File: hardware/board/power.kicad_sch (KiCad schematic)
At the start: 1 part, among them U4 RK809-5

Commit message: added stuff
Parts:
- added C10, C11, C12, C13, C14, C15, C20, C8, C9: 100nF X5R 10V, Capacitor_SMD:C_0402_1005Metric, symbol Device:C
- added C16, C17: 220pF C0G 25V, Capacitor_SMD:C_0402_1005Metric, symbol Device:C
- added C18: 1uF X5R 10V, Capacitor_SMD:C_0402_1005Metric, symbol Device:C
- added C19, C7: 10uF X5R 10V, Capacitor_SMD:C_0603_1608Metric, symbol Device:C
- added C21, C23, C3, C4, C5, C6: 10uF X5R 25V, Capacitor_SMD:C_0805_2012Metric, symbol Device:C
- added C22: 100pF C0G 50V, Capacitor_SMD:C_0402_1005Metric, symbol Device:C
- added C24: 4.7uF X5R 10V, Capacitor_SMD:C_0402_1005Metric, symbol Device:C
- added C25: 47nF X5R 25V, Capacitor_SMD:C_0402_1005Metric, symbol Device:C
- added C26, C27, C28: 10uF X5R 10V, Capacitor_SMD:C_0805_2012Metric, symbol Device:C
- added D1, D2, D3, D4, D5: BZT52C5V1_C173407, lcsc:SOD-123_L2.7-W1.6-LS3.7-RD, symbol lcsc:BZT52C5V1_C173407
- added D6, D7: ESD5344D, lcsc:DFN2510-10_L2.5-W1.0-P0.50-BL, symbol lcsc:ESD5344D
- added D8: LED, LED_SMD:LED_0603_1608Metric, symbol Device:LED
- added FB1: 3m 120@100MHz, Inductor_SMD:L_0603_1608Metric, symbol Device:FerriteBead
- added J2: USB_C_Receptacle, symbol Connector:USB_C_Receptacle
- added L1: L_Iron_Coupled_Small, lcsc:FILTER-SMD_4P-L2.0-W1.2-BL_DLW21H, symbol Device:L_Iron_Coupled_Small
- added L2: SLO0520H1R0MTT, lcsc:IND-SMD_L5.4-W5.1, symbol lcsc:SLO0520H1R0MTT
- added R10, R11: 0R 5%, Resistor_SMD:R_0201_0603Metric, symbol Device:R
- added R12, R9: 0R 5%, Resistor_SMD:R_0402_1005Metric, symbol Device:R
- added R13: 330R 5%, Resistor_SMD:R_0402_1005Metric, symbol Device:R
- added R14: 100R 5%, Resistor_SMD:R_0402_1005Metric, symbol Device:R
- added R15: 5.1K 1%, Resistor_SMD:R_0402_1005Metric, symbol Device:R
- added R16: 30K 1%, Resistor_SMD:R_0402_1005Metric, symbol Device:R
- added R3: 0R, Resistor_SMD:R_1206_3216Metric, symbol Device:R
- added R4: 470R 5%, Resistor_SMD:R_0805_2012Metric, symbol Device:R
- added R5: 10K 5%, Resistor_SMD:R_0402_1005Metric, symbol Device:R
- added R6: 15K 5%, Resistor_SMD:R_0402_1005Metric, symbol Device:R
- added R7, R8: 2.2R, Resistor_SMD:R_1206_3216Metric, symbol Device:R
- added U6: TMUXHS4212RKSR, lcsc:TQFN-20_L4.5-W2.5-P0.50-BL-EP3.0, symbol lcsc:TMUXHS4212RKSR
- added U7: FUSB302BMPX, Package_DFN_QFN:WQFN-14-1EP_2.5x2.5mm_P0.5mm_EP1.45x1.45mm, symbol Interface_USB:FUSB302BMPX
- added U8: BQ25890RTWR, lcsc:WQFN-24_L4.0-W4.0-P0.50-BL-EP, symbol lcsc:BQ25890RTWR
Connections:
- new net: R10.2, U6.8 (A1n)
- new net: R12.1, U8.9 (~{CE})
- new net: C25.1, L2.2, U8.19 (SW), U8.20 (SW)
- new net: R14.1, U8.10 (ILIM)
- new net: C13.2, U6.18 (B0n)
- new net: R13.1, U8.4 (STAT)
- new net: D8.1 (K), R13.2
- new net: C11.2, U6.14 (C0n)
- new net: C12.2, U6.15 (C0p)
- new net: C14.2, U6.19 (B0p)
- new net: R9.2, U6.2 (OEn)
- new net: R11.2, U6.7 (A1p)
- new net: L1.1, R7.1
- new net: L1.3, R8.1
- new net: C25.2, U8.21 (BTST)
- new net: C23.2, U8.23 (PMID)
- new net BATT_TS: C22.1, R15.2, R16.1, U8.11 (TS)
- new net BQ_OTG_EN_H_GPIO3_C3: U8.8 (OTG)
- new net CHG_INT_L_GPIO0_C2: U8.7 (INT)
- new net CHG_REF: C24.1, D8.2 (A), R15.1, U8.22 (REGN)
- new net GND: C10.2, C15.2, C16.2, C17.2, C18.2, C19.2, C20.2, C21.2, C22.2, C23.1, C24.2, C26.2, C27.2, C3.2, C4.2, C5.2, C6.2, C7.2, C8.2, C9.2, D1.2 (A), D2.2 (A), D3.2 (A), D4.2 (A), D5.2 (A), D6.3, D6.8, D7.3, D7.8, J2.A1 (GND), J2.A12 (GND), J2.B1 (GND), J2.B12 (GND), J2.S1 (SHIELD), R12.2, R14.2, R16.2, R6.1, R9.1, U6.11 (GND), U6.20 (GND), U6.21 (EPAD), U6.5 (GND), U7.15 (GND), U7.8 (GND), U7.9 (GND), U8.25 (PAD)
- new net I2C0_SCL_PMIC: U7.6 (SCL), U8.5 (SCL)
- new net I2C0_SDA_PMIC: U7.7 (SDA), U8.6 (SDA)
- new net TYPEC_0_CC1: C16.1, D4.1 (C), J2.A5 (CC1), U7.10 (CC1), U7.11 (CC1)
- new net TYPEC_0_CC2: C17.1, D5.1 (C), J2.B5 (CC2), U7.1 (CC2), U7.14 (CC2)
- new net TYPEC_0_DN: D3.1 (C), J2.A7 (D-), J2.B7 (D-), L1.4
- new net TYPEC_0_DP: D2.1 (C), J2.A6 (D+), J2.B6 (D+), L1.2
- new net TYPEC_0_SSRX1N: D6.5, D6.6, J2.B10 (RX1-), U6.16 (B1n)
- new net TYPEC_0_SSRX1P: D6.4, D6.7, J2.B11 (RX1+), U6.17 (B1p)
- new net TYPEC_0_SSRX2N: D7.5, D7.6, J2.A10 (RX2-), U6.12 (C1n)
- new net TYPEC_0_SSRX2P: D7.4, D7.7, J2.A11 (RX2+), U6.13 (C1p)
- new net TYPEC_0_SSTX1N: C13.1, D6.2, D6.9, J2.A3 (TX1-)
- new net TYPEC_0_SSTX1P: C14.1, D6.1, D6.10, J2.A2 (TX1+)
- new net TYPEC_0_SSTX2N: C11.1, D7.2, D7.9, J2.B3 (TX2-)
- new net TYPEC_0_SSTX2P: C12.1, D7.1, D7.10, J2.B2 (TX2+)
- new net TYPEC_0_SW_SEL_GPIO4_D2: U6.9 (SEL)
- new net USB3_OTG0_DP: R7.2, R8.2
- new net USB3_OTG0_SSRXN: R10.1
- new net USB3_OTG0_SSRXP: R11.1
- new net USB3_OTG0_SSTXN: U6.4 (A0n)
- new net USB3_OTG0_SSTXP: U6.3 (A0p)
- new net USB3_OTG0_VBUSDET: R5.2, R6.2
- new net USBCC_INT_L_GPIO0_C5: U7.5 (INT_N)
- new net VBUS_DC5V: D1.1 (C), R4.2, R5.1
- new net VBUS_TYPEC: C15.1, C5.1, C6.1, R3.2, R4.1, U7.2 (VBUS)
- new net VBUS_TYPEC_0: C21.1, C3.1, C4.1, J2.A4 (VBUS), J2.A9 (VBUS), J2.B4 (VBUS), J2.B9 (VBUS), R3.1, U8.1 (VBUS)
- new net VCC3V3_PMU: C18.1, U7.3 (VDD), U7.4 (VDD)
- new net VCC3V3_SYS: C19.1, C20.1, U7.12 (VCONN), U7.13 (VCONN)
- new net VCC3V3_U3_SW: C10.1, C7.1, C8.1, C9.1, FB1.2, U6.1 (RSVD1), U6.10 (RSVD2), U6.6 (VCC)
- new net VCC_3V3: FB1.1
- new net VCC_SYSIN: C26.1, C27.1, L2.1, U8.15 (SYS), U8.16 (SYS)
- no-connect marks 0 -> 6
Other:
- moved on the sheet: U4

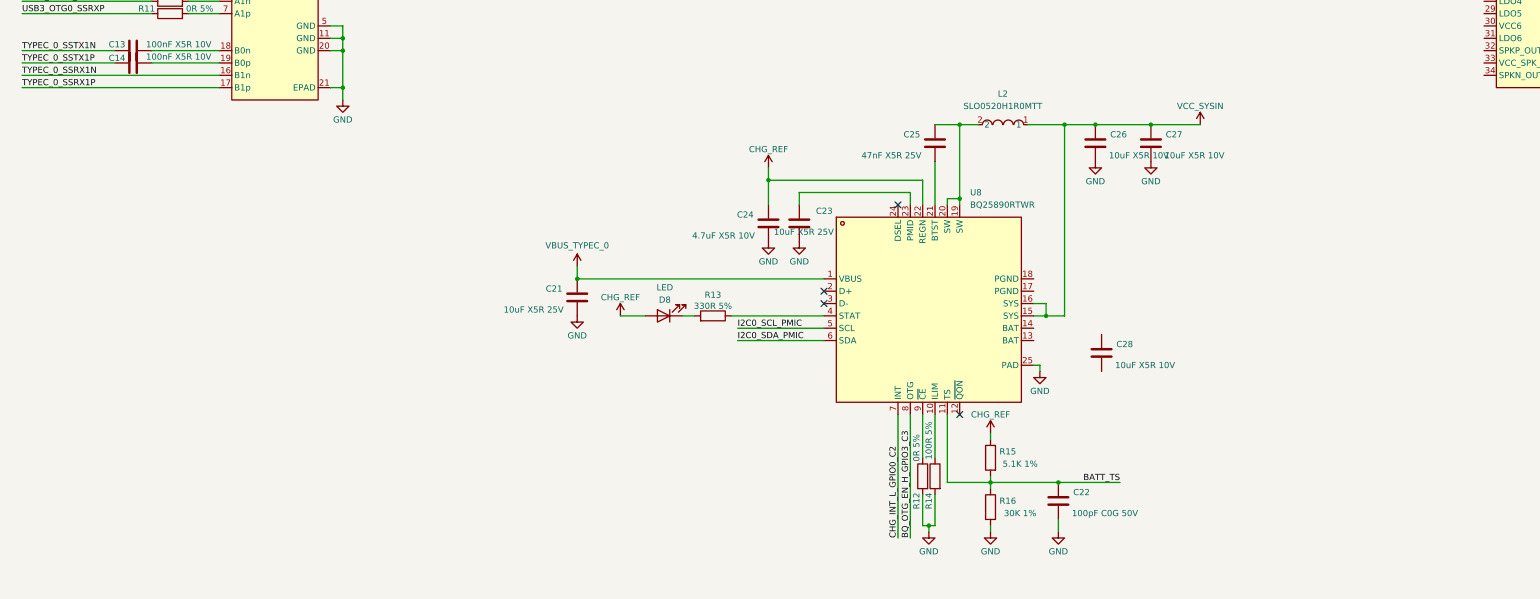
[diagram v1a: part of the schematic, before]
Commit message: added 3v3 buck and bat
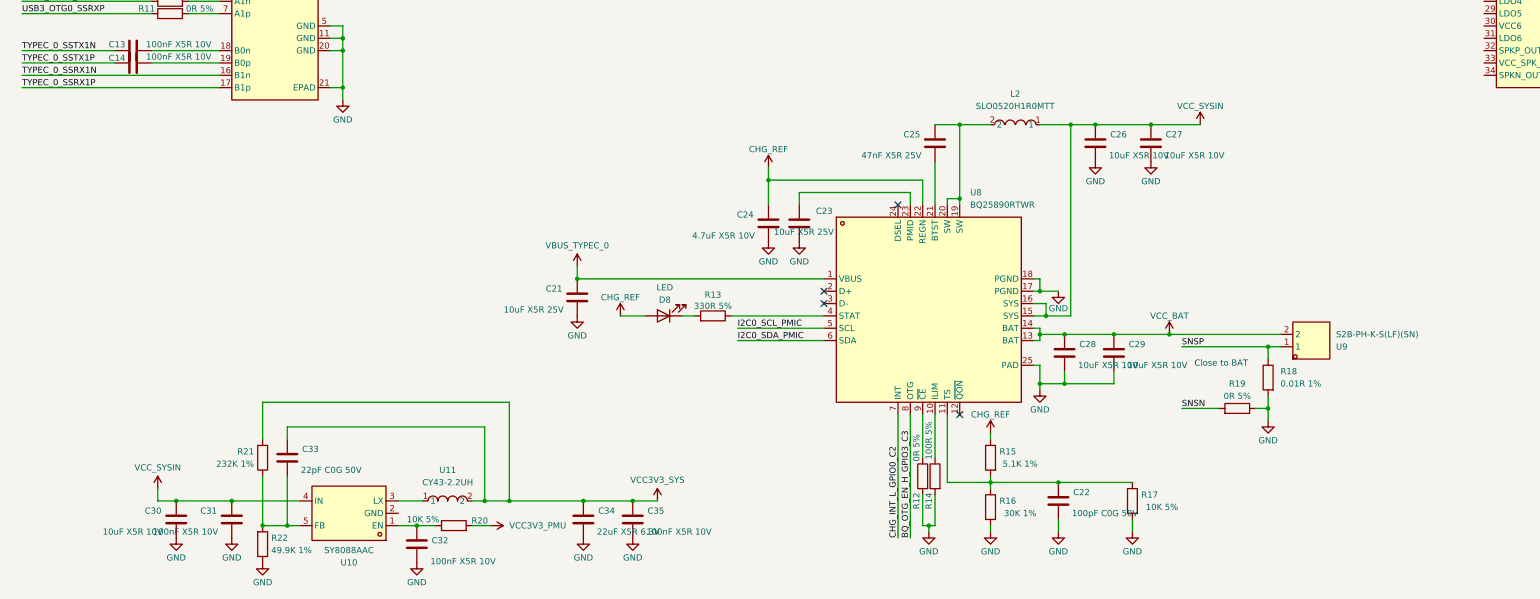
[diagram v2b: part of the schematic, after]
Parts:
- added C29: 10uF X5R 10V, Capacitor_SMD:C_0805_2012Metric, symbol Device:C
- added C30: 10uF X5R 10V, Capacitor_SMD:C_0603_1608Metric, symbol Device:C
- added C31, C32, C35: 100nF X5R 10V, Capacitor_SMD:C_0402_1005Metric, symbol Device:C
- added C33: 22pF C0G 50V, Capacitor_SMD:C_0402_1005Metric, symbol Device:C
- added C34: 22uF X5R 6.3V, Capacitor_SMD:C_0603_1608Metric, symbol Device:C
- added R17, R20: 10K 5%, Resistor_SMD:R_0402_1005Metric, symbol Device:R
- added R18: 0.01R 1%, Resistor_SMD:R_1206_3216Metric, symbol Device:R
- added R19: 0R 5%, Resistor_SMD:R_0402_1005Metric, symbol Device:R
- added R21: 232K 1%, Resistor_SMD:R_0402_1005Metric, symbol Device:R
- added R22: 49.9K 1%, Resistor_SMD:R_0402_1005Metric, symbol Device:R
- added U10: SY8088AAC, lcsc:SOT-23-5_L3.0-W1.7-P0.95-LS2.8-BR, symbol lcsc:SY8088AAC
- added U11: CY43-2.2UH, lcsc:IND-SMD_L4.5-W4.0_SLF0403-1, symbol lcsc:CY43-2.2UH
- added U9: S2B-PH-K-S(LF)(SN), lcsc:CONN-TH_S2B-PH-K-S-LF-SN, symbol lcsc:S2B-PH-K-S(LF)(SN)
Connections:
- net GND: now also C28.2, U8.17 (PGND), U8.18 (PGND), C29.2, C30.2, C31.2, C32.2, C34.2, C35.2, R17.2, R18.2, R19.1, R22.1
- net VCC3V3_PMU: now also R20.2
- net VCC3V3_SYS: now also C33.1, C34.1, C35.1, R21.2, U11.2
- net VCC_SYSIN: now also C30.1, C31.1, U10.4 (IN)
- net VCC_BAT: now reaches U8.13 (BAT)
- net VCC_BAT: now also C28.1, U8.14 (BAT), C29.1, U9.2
- net BATT_TS: no longer names the net of C22.1, R15.2, R16.1, U8.11 (TS)
- net BATT_TS: now also R17.1
- new net: C32.1, R20.1, U10.1 (EN)
- new net: U10.3 (LX), U11.1
- new net: C33.2, R21.1, R22.2, U10.5 (FB)
- new net SNSN: R19.2
- new net SNSP: R18.1, U9.1
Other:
- note added: "Close to BAT"
- moved on the sheet: C28, L2

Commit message: start pmic
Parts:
- removed U11: CY43-2.2UH, lcsc:IND-SMD_L4.5-W4.0_SLF0403-1, symbol lcsc:CY43-2.2UH
- added C36, C55, C56: 100nF X5R 16V, Capacitor_SMD:C_0402_1005Metric, symbol Device:C
- added C37: 10uF X5R 10V, Capacitor_SMD:C_0805_2012Metric, symbol Device:C
- added C38: 22pF C0G 50V, Capacitor_SMD:C_0402_1005Metric, symbol Device:C
- added C39: 22uF X5R 10V, Capacitor_SMD:C_0805_2012Metric, symbol Device:C
- added C40, C42, C53, C54: 100nF X5R 10V, Capacitor_SMD:C_0402_1005Metric, symbol Device:C
- added C41, C43: 10uF X5R 10V, Capacitor_SMD:C_0603_1608Metric, symbol Device:C
- added C44: 4.7uF X5R 6.3V, Capacitor_SMD:C_0402_1005Metric, symbol Device:C
- added C45, C46, C47, C48, C49: 1uF X5R 6.3V, Capacitor_SMD:C_0402_1005Metric, symbol Device:C
- added C50, C57: 1uF X5R 10V, Capacitor_SMD:C_0402_1005Metric, symbol Device:C
- added C51, C52: 20pF C0G 50V, Capacitor_SMD:C_0402_1005Metric, symbol Device:C
- added D9: SS32, Diode_SMD:D_SMA, symbol Diode:SS32
- added FB2, FB3: 120@100MHz 0.03R, Inductor_SMD:L_0603_1608Metric, symbol Device:FerriteBead
- added L3, L4: LVF404026-2R2M-N, lcsc:IND-SMD_L4.0-W4.0, symbol lcsc:LVF404026-2R2M-N
- added Q1: WPM3407-3/TR, lcsc:SOT-23-3_L3.0-W1.7-P0.95-LS2.9-BR, symbol lcsc:WPM3407-3_TR
- added Q2: SS8050, Package_TO_SOT_SMD:SOT-23, symbol Transistor_BJT:SS8050
- added Q3: WPM2015-3/TR_C7472861, lcsc:SOT-23-3_L2.9-W1.3-P1.90-LS2.4-BR, symbol lcsc:WPM2015-3_TR_C7472861
- added R23, R30: 100K 5%, Resistor_SMD:R_0402_1005Metric, symbol Device:R
- added R24, R26, R29, R34: 10K 5%, Resistor_SMD:R_0402_1005Metric, symbol Device:R
- added R25: 51K 5%, Resistor_SMD:R_0402_1005Metric, symbol Device:R
- added R27: 360K 1%, Resistor_SMD:R_0402_1005Metric, symbol Device:R
- added R28: 47K 1%, Resistor_SMD:R_0402_1005Metric, symbol Device:R
- added R31, R32, R33: 0R 5%, Resistor_SMD:R_0402_1005Metric, symbol Device:R
- added R35, R36: 22R 5%, Resistor_SMD:R_0402_1005Metric, symbol Device:R
- added R37, R39: 30K 1%, Resistor_SMD:R_0402_1005Metric, symbol Device:R
- added R38: 20K 1%, Resistor_SMD:R_0402_1005Metric, symbol Device:R
- added U12: SY7208ABC, lcsc:SOT-23-6_L2.9-W1.6-P0.95-LS2.8-BR, symbol lcsc:SY7208ABC
- added X2: Q13FC1350000400, lcsc:FC-135R_L3.2-W1.5, symbol lcsc:Q13FC1350000400
- FB1: value 3m 120@100MHz -> 120@100MHz 0.03R; LCSC (none) -> C85831
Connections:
- net GND: now also U4.47 (GNDREF), U4.69 (EP), C36.2, C37.2, C39.2, C40.2, C41.2, C42.2, C43.2, C44.2, C45.2, C46.2, C47.2, C48.2, C49.2, C50.2, C51.2, C52.2, C53.2, C54.2, C56.2, C57.2, Q2.2 (E), R23.1, R25.1, R28.1, R30.1, R38.1
- net I2C0_SCL_PMIC: now also R35.2
- net I2C0_SDA_PMIC: now also R36.2
- net SNSN: now also U4.63 (SNSN), C55.1
- net SNSP: now also U4.62 (SNSP), C55.2
- net VCC3V3_PMU: now also R34.1
- net VCC3V3_SYS: now also C41.1, C42.1, L4.2, Q3.2 (S)
- net VCC_3V3: now also C43.1, Q3.3 (D)
- net VCC_BAT: now also C56.1, R39.1
- net VCC_SYSIN: now also U4.45 (VCC_RTC), C36.1, C57.1, Q1.2 (S), R23.2
- net at U10.3 (LX): now also L4.1
- net at U4.1 (SCL): now also R35.1
- net at U4.2 (SDA): now also R36.1
- net at U4.46 (VREF): now also C50.1
- net PMIC_SLEEP_H: now reaches U4.49 (SLEEP)
- net PMIC_SLEEP_H: now also R29.1, R30.2
- net at U4.50 (XIN): now also C52.1, X2.1
- net at U4.51 (XOUT): now also C51.1, X2.2
- net PMIC_PWRON: now reaches U4.52 (PWRON)
- net PMIC_PWRON: now also C54.1
- net at U4.56 (BATDIV): now also R37.2, R38.2
- net RESETn: now reaches U4.67 (RESETB)
- net RESETn: now also C53.1, R34.2
- net at U4.68 (CLK32K): now also R33.2
- net PMIC_INT_L: now reaches U4.7 (INT)
- new net: Q2.1 (B), R25.2, R26.2
- new net: Q2.3 (C), R24.1
- new net: Q1.1 (G), R24.2
- new net: C38.2, R27.1, R28.2, U12.3 (FB)
- new net: C37.1, L3.1, Q1.3 (D), U12.4 (EN), U12.5 (IN)
- new net: Q3.1 (G), R29.2
- new net: R37.1, R39.2
- new net: D9.2 (A), L3.2, U12.1 (LX)
- new net PMIC_32KOUT_WIFI: R33.1
- new net USB5V0_EN_H_GPIO0_D6: R26.1
- new net VCCA_1V8: C49.1, R32.1
- new net VCCA_1V8_P: R32.2
- new net VCC_1V8: C47.1, C48.1, FB3.1, FB3.2
- new net VCC_5V0: C38.1, C39.1, C40.1, D9.1 (K), R27.2
- new net VDDA0V9_IMAGE: C45.1, FB2.2
- new net VDDA_0V9: C46.1, R31.1
- new net VDDA_0V9_P: R31.2
- new net VDD_LOGIC: C44.1, FB2.1
- no-connect marks 6 -> 8
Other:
- note added: "Close to BAT SNSP/N are differential"
- note removed: "Close to BAT"
- moved on the sheet: U4

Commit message: power done
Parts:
- added C100, C99: 680pF C0G 50V, Capacitor_SMD:C_0402_1005Metric, symbol Device:C
- added C58, C59, C60, C62, C63, C66, C67, C70, C77, C78: 22uF X5R 6.3V, Capacitor_SMD:C_0603_1608Metric, symbol Device:C
- added C61, C64, C68, C80, C97, C98: 100nF X5R 10V, Capacitor_SMD:C_0402_1005Metric, symbol Device:C
- added C65, C69, C71, C76, C89: 10uF X5R 10V, Capacitor_SMD:C_0603_1608Metric, symbol Device:C
- added C72, C73, C75, C79, C81, C82, C87, C88, C91, C93, C94: 1uF X5R 6.3V, Capacitor_SMD:C_0402_1005Metric, symbol Device:C
- added C74, C83, C84, C85: 1uF X5R 10V, Capacitor_SMD:C_0402_1005Metric, symbol Device:C
- added C86: 4.7uF X5R 6.3V, Capacitor_SMD:C_0402_1005Metric, symbol Device:C
- added C90: 4.7uF X5R 10V, Capacitor_SMD:C_0603_1608Metric, symbol Device:C
- added C92: 2.2uF X5R 10V, Capacitor_SMD:C_0402_1005Metric, symbol Device:C
- added C95, C96: 27pF C0G 50V, Capacitor_SMD:C_0402_1005Metric, symbol Device:C
- added FB4: 120@100MHz 0.03R, Inductor_SMD:L_0603_1608Metric, symbol Device:FerriteBead
- added FB5, FB6: 180@100M 1.5A, Inductor_SMD:L_0603_1608Metric, symbol Device:FerriteBead
- added L5, L6, L7, L8, L9: 470nH, symbol Device:L
- added R40, R41, R42: 100R 5%, Resistor_SMD:R_0402_1005Metric, symbol Device:R
- added R43: 47K 1%, Resistor_SMD:R_0402_1005Metric, symbol Device:R
- added R44: 120K 1%, Resistor_SMD:R_0402_1005Metric, symbol Device:R
- added R45: 0R 5%, Resistor_SMD:R_0402_1005Metric, symbol Device:R
- added R46: 30K 5%, Resistor_SMD:R_0402_1005Metric, symbol Device:R
- added R47: 100K 5%, Resistor_SMD:R_0402_1005Metric, symbol Device:R
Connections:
- net GND: now also C100.1, C58.2, C59.2, C60.2, C62.2, C63.2, C65.2, C66.2, C67.2, C69.2, C70.2, C71.2, C72.1, C73.1, C74.1, C75.1, C76.2, C77.2, C78.2, C79.1, C80.1, C81.1, C82.1, C83.1, C84.1, C85.1, C86.1, C87.2, C88.2, C89.2, C91.2, C92.2, C93.2, C94.2, C95.2, C96.2, C99.1, R44.1, R46.2
- net VBUS_DC5V: now also R47.2
- net VCC3V3_PMU: now also U4.31 (LDO6), C88.1
- net VCC3V3_SYS: now also U4.57 (VCC8), C75.2
- net VCC_1V8: now also C77.1, C78.1, L9.1, R45.2
- net VCC_5V0: now also FB4.1
- net VCC_SYSIN: now also U4.10 (VCC2), U4.11 (VCC1), U4.22 (VCC5), U4.24 (VCC3), U4.30 (VCC6), U4.4 (VCC7), U4.54 (VCC9), U4.66 (VCC4), C58.1, C65.1, C69.1, C72.2, C73.2, C74.2, C76.1
- net VDDA_0V9_P: now also U4.21 (LDO2), C84.2
- net VDD_LOGIC: now also U4.13 (FB1), C59.1, C60.1, C61.1, C61.2, L5.1, R40.1, R40.2
- net PMIC_XOUT: now reaches C52.1, X2.1
- net PMIC_XOUT: now also U4.51 (XOUT); no longer U4.50 (XIN)
- net PMIC_XIN: now reaches C51.1, X2.2
- net PMIC_XIN: now also U4.50 (XIN); no longer U4.51 (XOUT)
- net at U4.12 (SW1): now also L5.2
- net I2S1_LRCK_TX_M0_PMIC: now reaches U4.14 (LRCLK)
- net I2S1_SCLK_TX_M0_PMIC: now reaches U4.15 (BCLK)
- net I2S1_MCLK_M0_PMIC: now reaches U4.16 (MCLK)
- net I2S1_SDO0_M0_PMIC: now reaches U4.17 (SDI)
- net I2S1_SDI0_M0/PDM_SDI0_M0_PMIC: now reaches U4.18 (SDO/PDMDATA)
- net PDM_CLK0_M0_PMIC: now reaches U4.19 (PDMCLK)
- net VDDA0V9_PMU: now reaches U4.20 (LDO3)
- net VDDA0V9_PMU: now also C85.2
- net VDDA0V9_IMAGE_P: now reaches U4.23 (LDO1)
- net VDDA0V9_IMAGE_P: now also C83.2
- net at U4.25 (SW3): now also L8.2
- net VCC_DDR: now reaches U4.26 (VBUCK3)
- net VCC_DDR: now also C70.1, C71.1, L8.1, R43.2
- net at U4.27 (FB3): now also R43.1, R44.2
- net VCCIO_ACODEC: now reaches U4.28 (LDO4)
- net VCCIO_ACODEC: now also C86.2
- net VCCIO_SD: now reaches U4.29 (LDO5)
- net VCCIO_SD: now also C87.1
- net at U4.32 (SPKP_OUT): now also FB5.2
- net at U4.33 (VCC_SPK_HP): now also C89.1, FB4.2
- net at U4.34 (SPKN_OUT): now also FB6.2
- net at U4.35 (VCC_CPVSS): now also C92.1
- net at U4.36 (CPN): now also C90.2
- net at U4.37 (CPP): now also C90.1
- net at U4.38 (VCC_CPVDD): now also C91.1
- net HPL_OUT: now reaches U4.39 (HPL_OUT)
- net HP_SNS: now reaches U4.40 (HP_SNS)
- net HPR_OUT: now reaches U4.41 (HPR_OUT)
- net at U4.42 (MICIN): now also C96.1, C97.2
- net at U4.43 (MICIP): now also C95.1, C98.2
- net at U4.44 (VCC_1P8A): now also C94.1
- net at U4.48 (VCC_1P8D): now also C93.1
- net VCCA1V8_PMU: now reaches U4.5 (LDO8)
- net VCCA1V8_PMU: now also C82.2
- net at U4.53 (SW5): now also L9.2
- net VCC3V3_SD: now reaches U4.58 (SWOUT2)
- net VCC3V3_SD: now also C79.2
- net at U4.59 (FB5): now also R45.1
- net VCCA1V8_IMAGE_P: now reaches U4.6 (LDO9)
- net VCCA1V8_IMAGE_P: now also C81.2
- net at U4.61 (VDC): now also C80.2, R46.1, R47.1
- net VDD_NPU: now reaches U4.64 (FB4)
- net VDD_NPU: now also C66.1, C67.1, C68.1, C68.2, L7.1, R42.1, R42.2
- net at U4.65 (SW4): now also L7.2
- net VDD_GPU: now reaches U4.8 (FB2)
- net VDD_GPU: now also C62.1, C63.1, C64.1, C64.2, L6.1, R41.1, R41.2
- net at U4.9 (SW2): now also L6.2
- new net MIC1_INN: C97.1
- new net MIC1_INP: C98.1
- new net SPKN_OUT: C100.2, FB6.1
- new net SPKP_OUT: C99.2, FB5.1
- no-connect marks 8 -> 9
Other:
- note added: "Check feedback resistor depending on RAM type 47k is for LPDDR4"
- moved on the sheet: C52, C53, C54, C55, C56, C57, R34, R37, R38, R39, X2

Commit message: revised power
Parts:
- added C101: 1uF X5R 6.3V, Capacitor_SMD:C_0402_1005Metric, symbol Device:C
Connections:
- net GND: now also C101.1
- net VCCA_1V8_P: now also U4.3 (LDO7), C101.2
